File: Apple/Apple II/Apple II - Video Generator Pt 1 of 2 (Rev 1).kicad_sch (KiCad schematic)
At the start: 0 parts

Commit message: Finished Apple II - Sheet 15 - Video Generator Part 1 (Rev 1)
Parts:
- added A11, a11: 74LS74, symbol Apple II:A11_74LS74
- added A12: 74LS02, symbol Apple II:A12_74LS02
- added A?: 74LS151, symbol Apple II:A9_74LS151
- added A?: 74166, symbol Apple II:A3_74166
- added A?: 74LS194, symbol Apple II:A10_74LS194
- added B?: 74LS08, symbol Apple II:B11_74LS08
- added B?: 74LS194, symbol Apple II:B9_74LS194
- added B?: 74S86, symbol Apple II:B2_74S86
- added B?: 74LS74, symbol Apple II:B10_74LS74
- added B?: 74LS194, symbol Apple II:B4_74LS194
- added B?: 74LS11, symbol Apple II:B12_74LS11
- added B? (x2): 74LS02, symbol Apple II:B13_74LS02
- added C?: 0.1µF, symbol Device:C_Small
- added R?: 3.3M, symbol Device:R_US
- added R?: 12K, symbol Device:R_US
- added U? (x2): B8_74LS174, symbol Apple II:B8_74LS174
- added U?: A8_74LS257, symbol Apple II:A8_74LS257
- added U?: B11_74LS08, symbol Apple II:B11_74LS08
- added U?: B3_555, Package_SO:SOIC-8_3.9x4.9mm_P1.27mm, symbol Apple II:B3_555
- added U?: A5_2513, symbol Apple II:A5_2513
- added U?: B5_74LS174, symbol Apple II:B5_74LS174
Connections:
- new net: A12.8, A12.9, U?.2 (Q0), U?.5
- new net: U?.15 (Q5), U?.3 (D0)
- new net: B?.15 (Q0), U?.2 (0A), a11.12 (D)
- new net: A?.1 (D3), a11.9 (Q)
- new net: A12.10, A12.11
- new net: A11.1 (~{CLR}), A12.13, A?.9 (C)
- new net: B?.11, B?.5
- new net: B?.13, U?.3 (OUT)
- new net: B?.10 (S1), B?.10 (S1)
- new net: B?.11, B?.11
- new net: A?.12 (D7), B?.13 (Q2)
- new net: A?.13 (D6), B?.15 (Q0), B?.7 (DSL), U?.3 (1A)
- new net: B?.9 (S0), B?.9 (S0)
- new net: C?.2, R?.1, U?.2 (TR), U?.6 (TH)
- new net: R?.1, R?.2, U?.7 (DIS)
- new net: A?.3 (D1), A?.4 (D0), B?.11
- new net: A?.1 (SER.IN), A?.12 (Q3), B?.12
- new net: A?.13 (Q_{H}), B?.13
- new net: A?.5 (Y), B?.2 (D)
- new net: A11.6 (~{Q}), U?.1 (S)
- new net: A?.10 (B), A?.15 (Q0)
- new net: A?.11 (A), A?.14 (Q1)
- new net: A?.14 (D5), B?.13 (Q2)
- new net: A?.15 (D4), A?.2 (D2)
- new net: A?.13 (Q2), A?.7 (~{ST})
- new net: B?.10 (S1), U?.9 (ZC)
- new net: B?.7 (DSL), U?.4 (ZA)
- new net: A?.10 (E), U?.6 (D3)
- new net: A?.11 (F), U?.7 (D4)
- new net: A?.12 (G), U?.8 (D5)
- new net: A?.2 (A), A?.6 (D3), B?.4
- new net: A?.4 (C), U?.4 (D1)
- new net: A?.5 (D), U?.5 (D2)
- new net: A?.4 (D1), U?.12 (ZD)
- new net: U?.14 (D4), U?.2 (Q0), U?.6 (1B)
- new net: A?.3 (D0), U?.7 (ZB)
- new net: B?.11, B?.6
- new net: B?.13, U?.3 (D0)
- new net +5V: R?.2, U?.4 (~{R}), U?.8 (VCC)
- new net 14M: A?.11 (Cp), A?.7 (CL2), B?.11, B?.3 (CLK), a11.11 (CLK)
- new net 7M_{36}: A?.6 (CL1)
- new net BLANKING: A?.5 (D2)
- new net DL0: B?.3 (D0), U?.17 (A4)
- new net DL1: B?.4 (D1), U?.18 (A5)
- new net DL2: B?.5 (D2), U?.19 (A6)
- new net DL3: B?.6 (D3), U?.20 (A7)
- new net DL4: B?.3 (D0), U?.21 (A8)
- new net DL5: B?.4 (D1), U?.22 (A9)
- new net DL6: B?.12, B?.5 (D2)
- new net DL7: B?.6, B?.6 (D3), U?.13 (1D)
- new net Earth: A11.4 (~{P}), A?.14 (H), A?.3 (B), C?.1, U?.1 (GND), U?.10 (GND), U?.11 (~{CE}), U?.15 (~{E})
- new net H0: U?.14 (0D)
- new net HIRES: U?.6
- new net HIRES MODE: A12.12, U?.4
- new net LD194: A?.10 (S1), A?.9 (S0), B?.9 (S0)
- new net MIX MODE: B?.5
- new net SOFT 5: A11.2 (D), A11.3 (CLK), A?.9 (~{CLR}), B?.1 (~{CLR}), B?.4 (~{P}), U?.1 (~{CLR}), U?.1 (~{CLR}), U?.1 (~{CLR}), U?.11 (0C), a11.10 (~{P}), a11.13 (~{CLR})
- new net TEXT MODE: B?.12
- new net V2: B?.3
- new net V4: B?.4
- new net VA: U?.14 (A1)
- new net VB: U?.15 (A2)
- new net VC: U?.16 (A3), U?.5 (0B)
- new net VIDEO_DATA: B?.5 (Q)
- new net ~{7M}: U?.10 (1C)
- new net ~{LDPS}: A?.15 (~{LD})
- new net ~{RAS}: U?.9 (Cp), U?.9 (Cp), U?.9 (Cp)
- no-connect marks 0 -> 3
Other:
- note added: "FROM CLOCK GENERATOR"
- note added: "FROM ON-BOARD I/O"
- note added: "FROM PART 2"
- note added: "FROM RAM"
- note added: "FROM VIDEO ADDRESS GENERATOR"
- note added: "TO MEMORY ADDRESS"
- note added: "TO PART 2"
- title: (none) -> Apple II - Video Generator Part 1

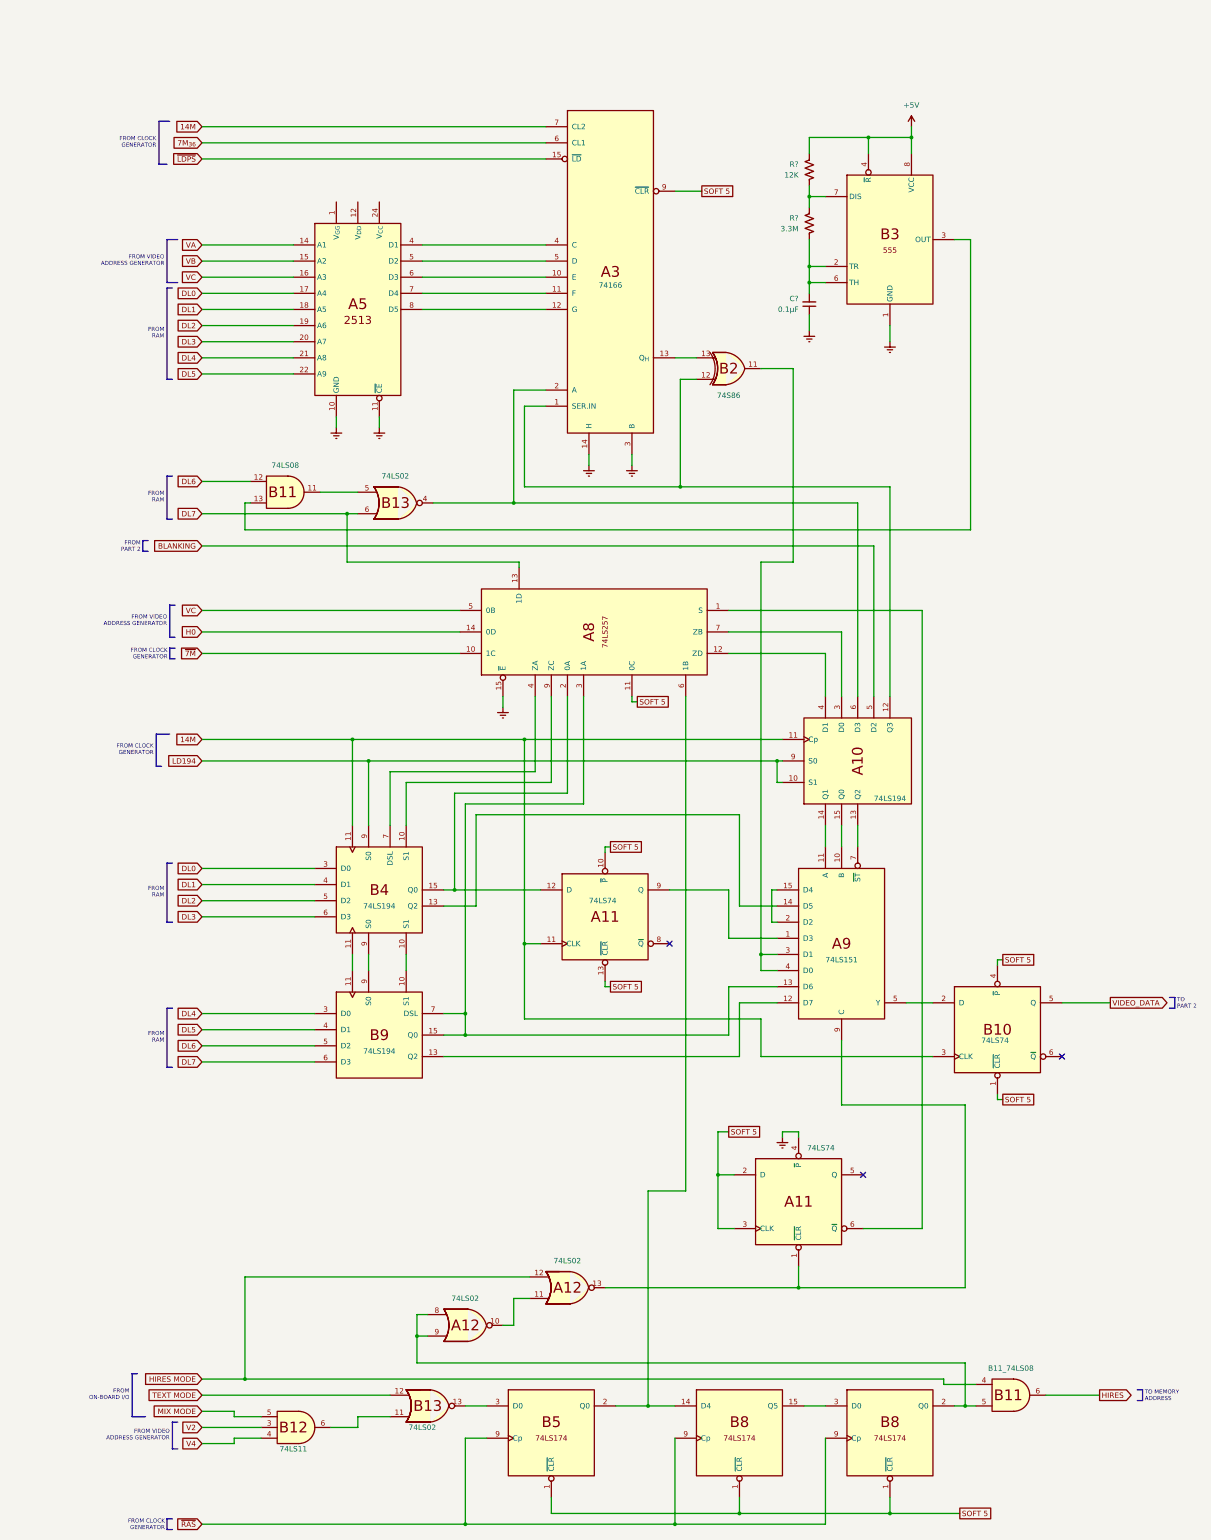
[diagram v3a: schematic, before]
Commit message: Finished Apple II - Sheet 16 - Video Generator Part 1 (Rev 7, RFI)
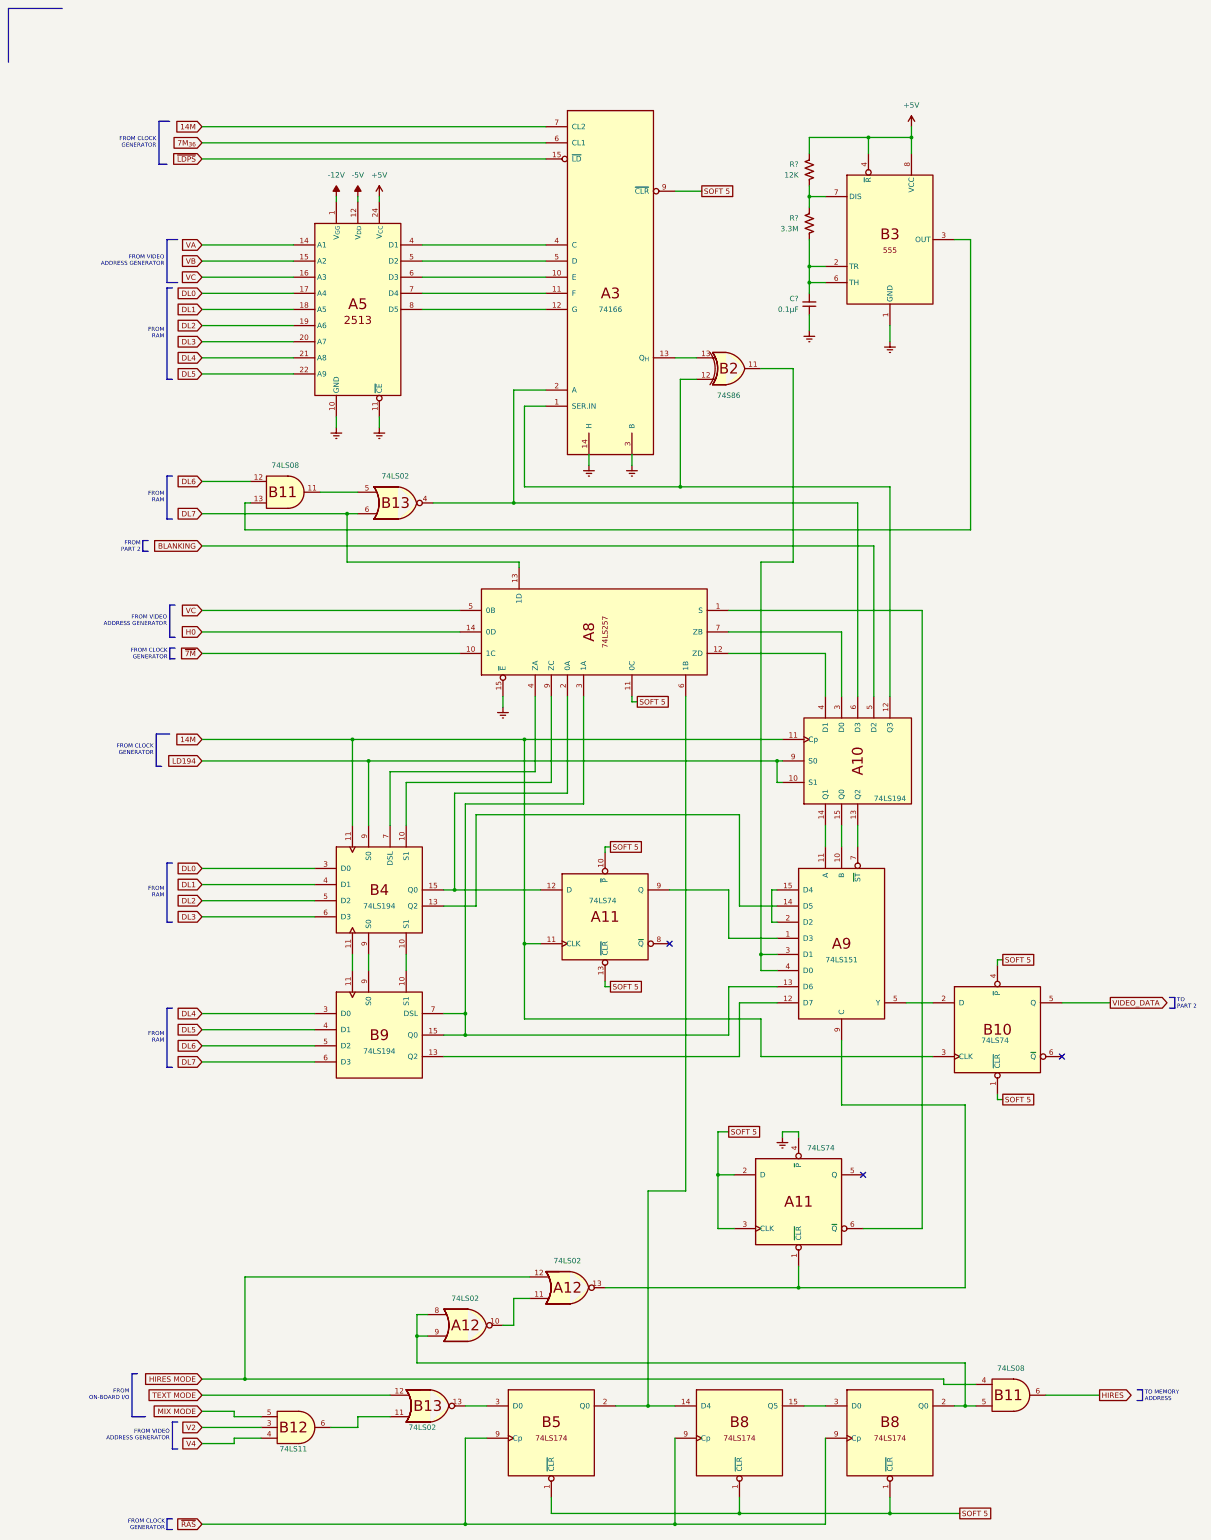
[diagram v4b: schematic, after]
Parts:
- B11: renamed from U?; value B11_74LS08 -> 74LS08
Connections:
- net +5V: now also U?.24 (V_{CC})
- net -12V: now reaches U?.1 (V_{GG})
- net -5V: now reaches U?.12 (V_{DD})
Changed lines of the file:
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@@
+    (stroke (width 0) (type default) (color 0 0 0 0))
+  )
+  (wire (pts (xy 82.55 44.45) (xy 82.55 45.72))
     (stroke (width 0) (type default) (color 0 0 0 0))
   )
@@
     (stroke (width 0) (type solid) (color 0 0 0 0))
   )
+  (wire (pts (xy 87.63 44.45) (xy 87.63 45.72))
+    (stroke (width 0) (type default) (color 0 0 0 0))
+  )
   (polyline (pts (xy 38.735 66.04) (xy 37.465 66.04))
     (stroke (width 0) (type solid) (color 0 0 0 0))
@@
     (stroke (width 0) (type solid) (color 0 0 0 0))
   )
+  (polyline (pts (xy 0 0) (xy 0 12.7))
+    (stroke (width 0) (type default) (color 0 0 0 0))
+  )
   (wire (pts (xy 212.09 234.95) (xy 218.44 234.95))
     (stroke (width 0) (type default) (color 0 0 0 0))
@@
     (stroke (width 0) (type default) (color 0 0 0 0))
   )
+  (polyline (pts (xy 12.7 0) (xy 0 0))
+    (stroke (width 0) (type default) (color 0 0 0 0))
+  )
   (wire (pts (xy 172.72 234.95) (xy 181.61 234.95))
+    (stroke (width 0) (type default) (color 0 0 0 0))
+  )
+  (wire (pts (xy 77.47 44.45) (xy 77.47 45.72))
     (stroke (width 0) (type default) (color 0 0 0 0))
   )
@@
     (pin "1")
   )
+  (symbol (lib_id "power:-12V") (at 77.47 44.45 0) (unit 1)
+    (in_bom yes) (on_board yes) (fields_autoplaced)
+    (property "Reference" "#PWR?" (id 0) (at 77.47 41.91 0)
+      (effects (font (size 1.27 1.27)) hide)
+    )
+    (property "Value" "-12V" (id 1) (at 77.47 39.37 0))
+    (property "Footprint" "" (id 2) (at 77.47 44.45 0)
+      (effects (font (size 1.27 1.27)) hide)
+    )
+    (property "Datasheet" "" (id 3) (at 77.47 44.45 0)
+      (effects (font (size 1.27 1.27)) hide)
+    )
+    (pin "1")
+  )
   (symbol (lib_id "power:Earth") (at 189.23 76.2 0) (unit 1)
     (in_bom yes) (on_board yes) (fields_autoplaced)
@@
       (effects (font (size 1.27 1.27)) hide)
     )
-    (property "Value" "74166" (id 1) (at 142.24 65.405 0))
+    (property "Value" "74166" (id 1) (at 142.24 71.12 0))
     (property "Footprint" "" (id 2) (at 132.08 24.13 0)
       (effects (font (size 1.27 1.27)) hide)
@@
     (pin "9")
   )
+  (symbol (lib_id "power:+5V") (at 87.63 44.45 0) (unit 1)
+    (in_bom yes) (on_board yes) (fields_autoplaced)
+    (property "Reference" "#PWR?" (id 0) (at 87.63 48.26 0)
+      (effects (font (size 1.27 1.27)) hide)
+    )
+    (property "Value" "+5V" (id 1) (at 87.63 39.37 0))
+    (property "Footprint" "" (id 2) (at 87.63 44.45 0)
+      (effects (font (size 1.27 1.27)) hide)
+    )
+    (property "Datasheet" "" (id 3) (at 87.63 44.45 0)
+      (effects (font (size 1.27 1.27)) hide)
+    )
+    (pin "1")
+  )
   (symbol (lib_id "Apple II:B11_74LS08") (at 236.22 327.66 0) (unit 2)
     (in_bom yes) (on_board yes) (fields_autoplaced)
-    (property "Reference" "U?" (id 0) (at 204.47 306.07 0)
-      (effects (font (size 1.27 1.27)) hide)
-    )
-    (property "Value" "B11_74LS08" (id 1) (at 236.855 321.31 0))
+    (property "Reference" "B11" (id 0) (at 204.47 306.07 0)
+      (effects (font (size 1.27 1.27)) hide)
+    )
+    (property "Value" "74LS08" (id 1) (at 236.855 321.31 0))
     (property "Footprint" "" (id 2) (at 237.49 327.66 0)
       (effects (font (size 1.27 1.27)) hide)
@@
     (pin "13")
   )
+  (symbol (lib_id "power:-5V") (at 82.55 44.45 0) (unit 1)
+    (in_bom yes) (on_board yes) (fields_autoplaced)
+    (property "Reference" "#PWR?" (id 0) (at 82.55 41.91 0)
+      (effects (font (size 1.27 1.27)) hide)
+    )
+    (property "Value" "-5V" (id 1) (at 82.55 39.37 0))
+    (property "Footprint" "" (id 2) (at 82.55 44.45 0)
+      (effects (font (size 1.27 1.27)) hide)
+    )
+    (property "Datasheet" "" (id 3) (at 82.55 44.45 0)
+      (effects (font (size 1.27 1.27)) hide)
+    )
+    (pin "1")
+  )
   (symbol (lib_id "Apple II:B13_74LS02") (at 97.79 330.2 0) (mirror x) (unit 4)

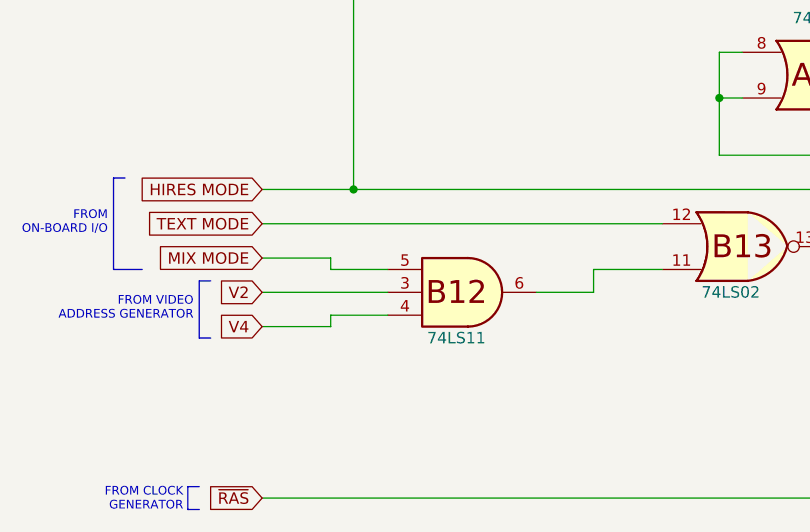
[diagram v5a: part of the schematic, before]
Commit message: Finished Apple II - Single Piece Keyboard
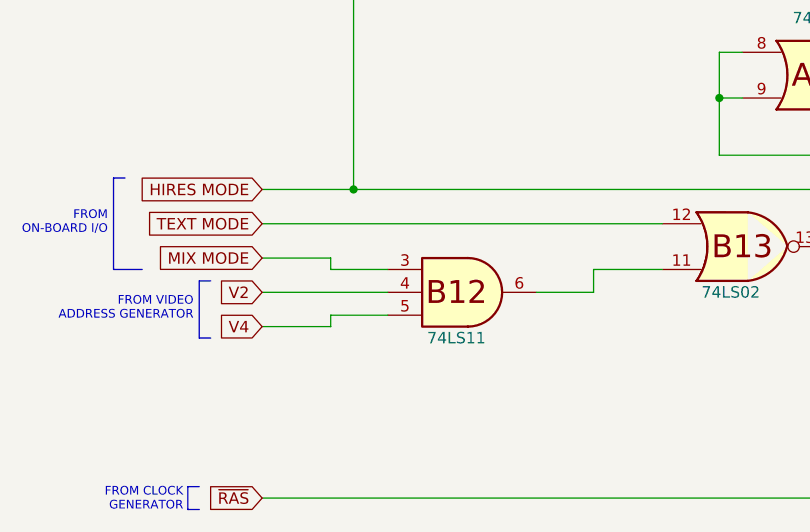
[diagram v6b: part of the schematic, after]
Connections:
- net MIX MODE: now also B?.3; no longer B?.5
- net V2: now also B?.4; no longer B?.3
- net V4: now also B?.5; no longer B?.4
